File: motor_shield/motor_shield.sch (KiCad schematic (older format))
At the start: 14 parts

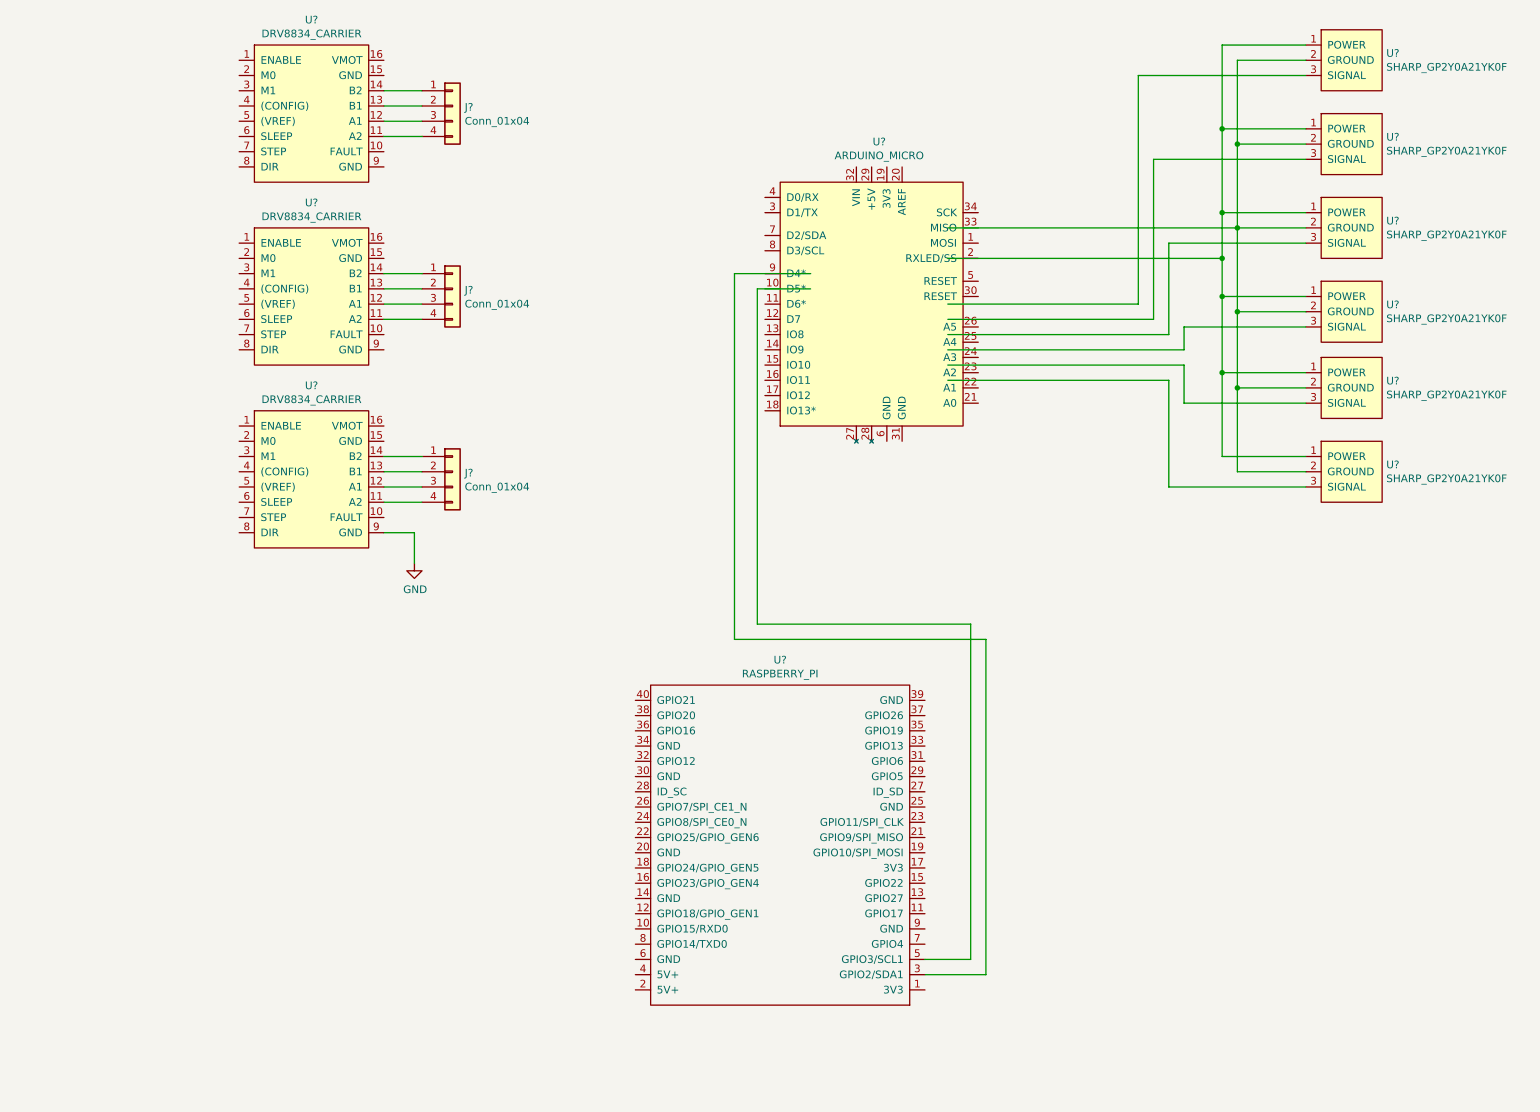
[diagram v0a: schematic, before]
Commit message: Removed buses, wired everything up more simple like
Seemed easier for me to visual the connections w/o the bus lines
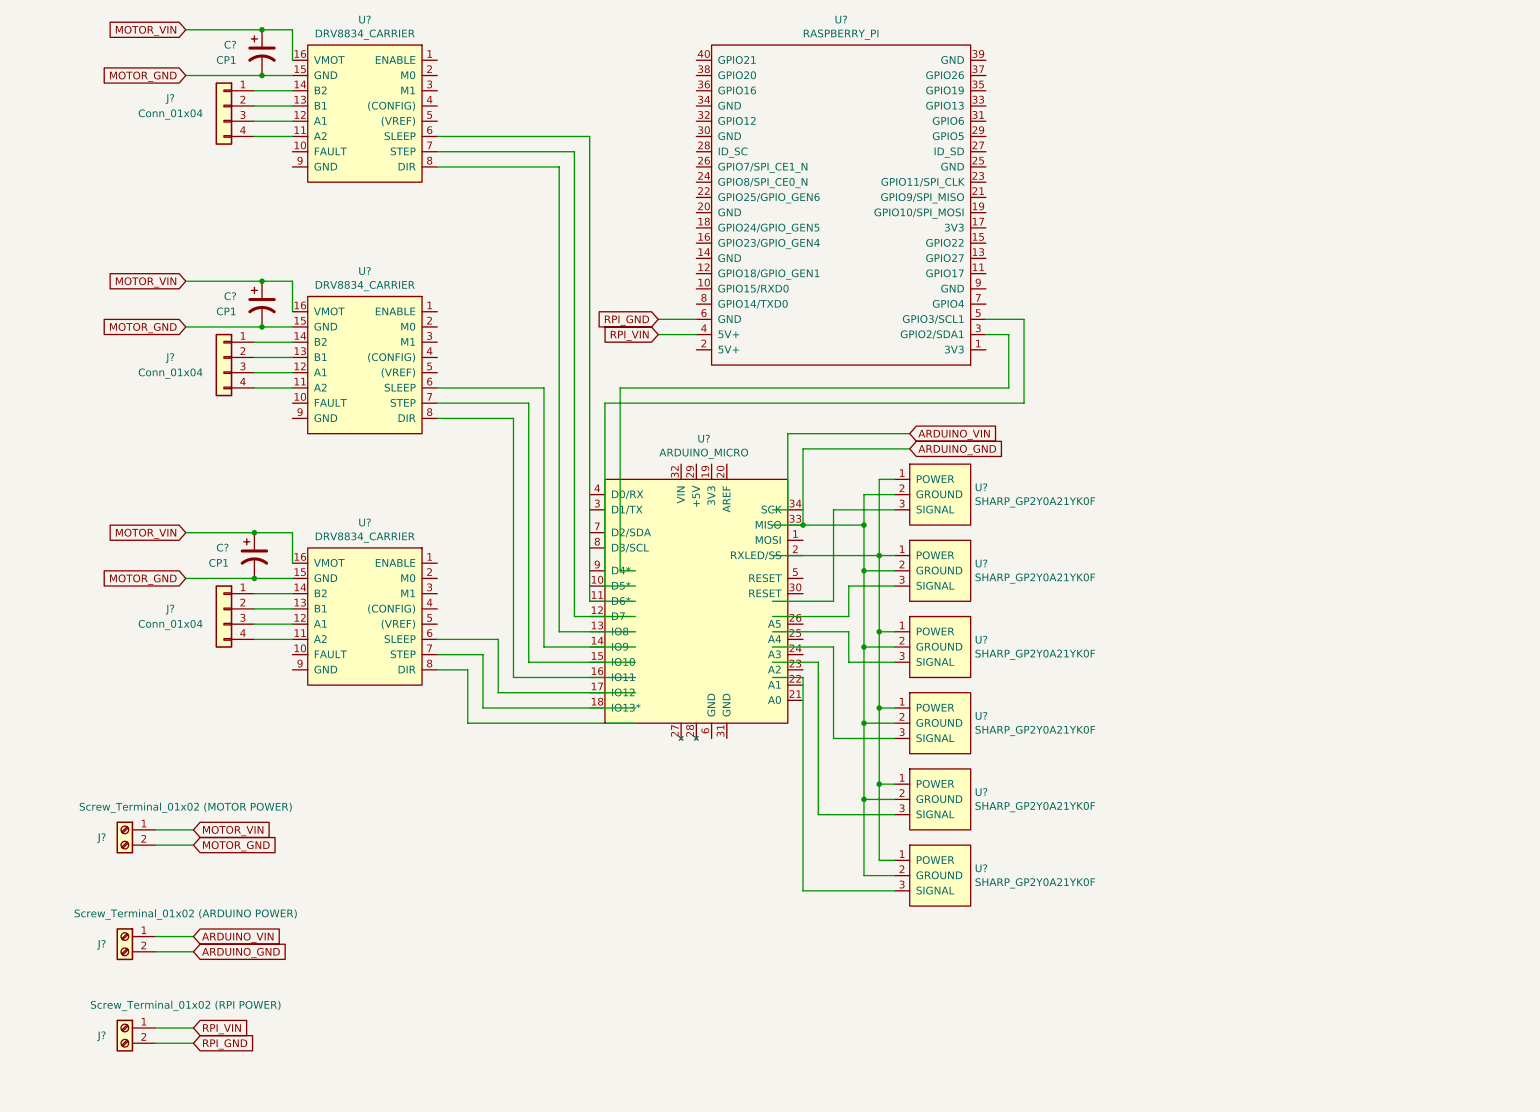
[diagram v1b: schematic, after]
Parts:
- removed J? (x2): Conn_01x04, symbol Connector_Generic:Conn_01x04
- removed U? (x2): DRV8834_CARRIER, symbol CATPOO:DRV8834_CARRIER
- removed U? (x5): SHARP_GP2Y0A21YK0F, symbol CATPOO:SHARP_GP2Y0A21YK0F
- added C? (x3): CP1, symbol Device:CP1
- added J?: Screw_Terminal_01x02 (MOTOR POWER), symbol Connector:Screw_Terminal_01x02
- added J? (x2): Conn_01x04, symbol Connector_Generic:Conn_01x04
- added J?: Screw_Terminal_01x02 (ARDUINO POWER), symbol Connector:Screw_Terminal_01x02
- added J?: Screw_Terminal_01x02 (RPI POWER), symbol Connector:Screw_Terminal_01x02
- added U? (x5): SHARP_GP2Y0A21YK0F, symbol CATPOO:SHARP_GP2Y0A21YK0F
- added U? (x2): DRV8834_CARRIER, symbol CATPOO:DRV8834_CARRIER
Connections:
- net labels added: ARDUINO_GND, ARDUINO_VIN, MOTOR_GND, MOTOR_VIN, RPI_GND, RPI_VIN
- net labels removed: GND
- wire segments 67 -> 121
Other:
- moved on the sheet: J?, U?

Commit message: Assigned footprints, ERC clean up
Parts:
- removed J?: Screw_Terminal_01x02 (ARDUINO POWER), symbol Connector:Screw_Terminal_01x02
- removed J?: Screw_Terminal_01x02 (RPI POWER), symbol Connector:Screw_Terminal_01x02
- removed U? (x4): SHARP_GP2Y0A21YK0F, symbol CATPOO:SHARP_GP2Y0A21YK0F
- added C4: CP1, Capacitor_THT:CP_Radial_D10.0mm_P5.00mm, symbol Device:CP1
- added C5: CP1_Small, Capacitor_THT:CP_Radial_D5.0mm_P2.50mm, symbol Device:CP1_Small
- added J2, J3: Screw_Terminal_01x02, CATPOO:TerminalBlock_Pololu-2_P5.00mm, symbol Connector:Screw_Terminal_01x02
- added U10, U11, U8, U9: SHARP_GP2Y0A21YK0F, Connector_JST:JST_XH_B03B-XH-A_1x03_P2.50mm_Vertical, symbol CATPOO:SHARP_GP2Y0A21YK0F
- C1, C2, C3: renamed from C?; footprint (none) -> Capacitor_THT:CP_Radial_D10.0mm_P5.00mm
- J1: renamed from J?; value Screw_Terminal_01x02 (MOTOR POWER) -> Screw_Terminal_01x02; footprint (none) -> CATPOO:TerminalBlock_Pololu-2_P5.00mm
- J4, J5, J6: renamed from J?; footprint (none) -> Connector_JST:JST_XH_B04B-XH-A_1x04_P2.50mm_Vertical
- U1, U2, U3: renamed from U?; footprint (none) -> CATPOO:DRV8834
- U4: renamed from U?; footprint (none) -> CATPOO:DIP-34_600
- U5: renamed from U?; footprint (none) -> Connector_PinHeader_2.54mm:PinHeader_2x20_P2.54mm_Vertical
- U6, U7: renamed from U?; footprint (none) -> Connector_JST:JST_XH_B03B-XH-A_1x03_P2.50mm_Vertical
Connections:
- net labels added: +5V, +7.5V, GND
- wire segments 121 -> 145
- no-connect marks 0 -> 65
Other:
- moved on the sheet: J1, U5, U6, U7

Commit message: WIP board layout
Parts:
- C1: renamed from C2; footprint Capacitor_THT:CP_Radial_D10.0mm_P5.00mm -> Capacitor_THT:CP_Radial_D8.0mm_P3.50mm
- C2: renamed from C3; value CP1 -> CP2; footprint Capacitor_THT:CP_Radial_D10.0mm_P5.00mm -> Capacitor_THT:CP_Radial_D8.0mm_P3.50mm
- C3: renamed from C1; value CP1 -> CP3; footprint Capacitor_THT:CP_Radial_D10.0mm_P5.00mm -> Capacitor_THT:CP_Radial_D8.0mm_P3.50mm
- C4: footprint Capacitor_THT:CP_Radial_D10.0mm_P5.00mm -> Capacitor_THT:CP_Radial_D8.0mm_P2.50mm
- U4: footprint CATPOO:DIP-34_600 -> CATPOO:ARDUINO_MICRO
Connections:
- net labels removed: +5V, +7.5V
- wire segments 145 -> 136
- no-connect marks 65 -> 66
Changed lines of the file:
@@
 EESchema Schematic File Version 4
+LIBS:motor_shield-cache
 EELAYER 26 0
 EELAYER END
@@
 F 0 "U4" H 4750 5615 50  0000 C CNN
 F 1 "ARDUINO_MICRO" H 4750 5524 50  0000 C CNN
-F 2 "CATPOO:DIP-34_600" H 4750 4550 50  0001 C CNN
+F 2 "CATPOO:ARDUINO_MICRO" H 4750 4550 50  0001 C CNN
 F 3 "" H 4750 4550 50  0001 C CNN
 	1    4750 4550
@@
 $EndComp
 $Comp
-L Device:CP1 C2
+L Device:CP1 C1
 U 1 1 5C82394E
 P 1850 950
-F 0 "C2" H 1600 1000 50  0000 L CNN
+F 0 "C1" H 1600 1000 50  0000 L CNN
 F 1 "CP1" H 1550 900 50  0000 L CNN
-F 2 "Capacitor_THT:CP_Radial_D10.0mm_P5.00mm" H 1850 950 50  0001 C CNN
+F 2 "Capacitor_THT:CP_Radial_D8.0mm_P3.50mm" H 1850 950 50  0001 C CNN
 F 3 "~" H 1850 950 50  0001 C CNN
 	1    1850 950
@@
 $EndComp
 $Comp
-L Device:CP1 C3
+L Device:CP1 C2
 U 1 1 5C837FE6
 P 1850 2600
-F 0 "C3" H 1600 2650 50  0000 L CNN
-F 1 "CP1" H 1550 2550 50  0000 L CNN
-F 2 "Capacitor_THT:CP_Radial_D10.0mm_P5.00mm" H 1850 2600 50  0001 C CNN
+F 0 "C2" H 1600 2650 50  0000 L CNN
+F 1 "CP2" H 1550 2550 50  0000 L CNN
+F 2 "Capacitor_THT:CP_Radial_D8.0mm_P3.50mm" H 1850 2600 50  0001 C CNN
 F 3 "~" H 1850 2600 50  0001 C CNN
 	1    1850 2600
@@
 $EndComp
 $Comp
-L Device:CP1 C1
+L Device:CP1 C3
 U 1 1 5C83805A
 P 1800 4250
-F 0 "C1" H 1550 4300 50  0000 L CNN
-F 1 "CP1" H 1500 4200 50  0000 L CNN
-F 2 "Capacitor_THT:CP_Radial_D10.0mm_P5.00mm" H 1800 4250 50  0001 C CNN
+F 0 "C3" H 1550 4300 50  0000 L CNN
+F 1 "CP3" H 1500 4200 50  0000 L CNN
+F 2 "Capacitor_THT:CP_Radial_D8.0mm_P3.50mm" H 1800 4250 50  0001 C CNN
 F 3 "~" H 1800 4250 50  0001 C CNN
 	1    1800 4250
@@
 	1850 2450 1350 2450
 Connection ~ 1850 2450
+Text GLabel 1400 6800 3    50   Input ~ 0
+MOTOR_VIN
 Text GLabel 1300 6800 3    50   Input ~ 0
-MOTOR_VIN
-Text GLabel 1400 6800 3    50   Input ~ 0
 MOTOR_GND
+Text GLabel 3100 6800 3    50   Input ~ 0
+ARDUINO_VIN
 Text GLabel 3000 6800 3    50   Input ~ 0
-ARDUINO_VIN
-Text GLabel 3100 6800 3    50   Input ~ 0
 ARDUINO_GND
 Text GLabel 6100 3450 2    50   Input ~ 0
@@
 Wire Wire Line
 	5600 3450 5600 4050
+Text GLabel 4800 6800 3    50   Input ~ 0
+RPI_VIN
 Text GLabel 4700 6800 3    50   Input ~ 0
-RPI_VIN
-Text GLabel 4800 6800 3    50   Input ~ 0
 RPI_GND
 Text GLabel 4450 2800 0    50   Input ~ 0
@@
 F 0 "C4" H 4800 2900 50  0000 L CNN
 F 1 "CP1" H 4800 2450 50  0000 L CNN
-F 2 "Capacitor_THT:CP_Radial_D10.0mm_P5.00mm" H 4850 2650 50  0001 C CNN
+F 2 "Capacitor_THT:CP_Radial_D8.0mm_P2.50mm" H 4850 2650 50  0001 C CNN
 F 3 "~" H 4850 2650 50  0001 C CNN
 	1    4850 2650
@@
 Wire Wire Line
 	4650 2500 4850 2500
-$Comp
-L power:GND #PWR0103
-U 1 1 5CA8F279
-P 1550 6650
-F 0 "#PWR0103" H 1550 6400 50  0001 C CNN
-F 1 "GND" H 1555 6477 50  0000 C CNN
-F 2 "" H 1550 6650 50  0001 C CNN
-F 3 "" H 1550 6650 50  0001 C CNN
-	1    1550 6650
-	1    0    0    -1
-$EndComp
-$Comp
-L power:+7.5V #PWR0105
-U 1 1 5CA9E4FA
-P 1100 6650
-F 0 "#PWR0105" H 1100 6500 50  0001 C CNN
-F 1 "+7.5V" H 1115 6823 50  0000 C CNN
-F 2 "" H 1100 6650 50  0001 C CNN
-F 3 "" H 1100 6650 50  0001 C CNN
-	1    1100 6650
-	1    0    0    -1
-$EndComp
-$Comp
-L power:+5V #PWR0106
-U 1 1 5CAA3A9E
-P 4500 6650
-F 0 "#PWR0106" H 4500 6500 50  0001 C CNN
-F 1 "+5V" H 4515 6823 50  0000 C CNN
-F 2 "" H 4500 6650 50  0001 C CNN
-F 3 "" H 4500 6650 50  0001 C CNN
-	1    4500 6650
-	1    0    0    -1
-$EndComp
 $Comp
 L power:GND #PWR0107
@@
 NoConn ~ 3000 4300
 NoConn ~ 5150 2900
-$Comp
-L power:PWR_FLAG #FLG0102
-U 1 1 5CD0B3E5
-P 800 6650
-F 0 "#FLG0102" H 800 6725 50  0001 C CNN
-F 1 "PWR_FLAG" H 800 6824 50  0000 C CNN
-F 2 "" H 800 6650 50  0001 C CNN
-F 3 "~" H 800 6650 50  0001 C CNN
-	1    800  6650
-	1    0    0    -1
-$EndComp
 NoConn ~ 7050 2600
-Wire Wire Line
-	1550 6650 1400 6650
-Wire Wire Line
-	1300 6650 1100 6650
-Wire Wire Line
-	1100 6650 800  6650
-Connection ~ 1100 6650
-Wire Wire Line
-	1400 6800 1400 6650
-Connection ~ 1400 6650
-Wire Wire Line
-	1300 6800 1300 6650
-Connection ~ 1300 6650
 $Comp
 L Connector:Screw_Terminal_01x02 J2
@@
 	0    1    -1   0
 $EndComp
-$Comp
-L power:GND #PWR02
-U 1 1 5CDAA99A
-P 3250 6650
-F 0 "#PWR02" H 3250 6400 50  0001 C CNN
-F 1 "GND" H 3255 6477 50  0000 C CNN
-F 2 "" H 3250 6650 50  0001 C CNN
-F 3 "" H 3250 6650 50  0001 C CNN
-	1    3250 6650
-	1    0    0    -1
-$EndComp
-$Comp
-L power:+7.5V #PWR01
-U 1 1 5CDAA9A0
-P 2800 6650
-F 0 "#PWR01" H 2800 6500 50  0001 C CNN
-F 1 "+7.5V" H 2815 6823 50  0000 C CNN
-F 2 "" H 2800 6650 50  0001 C CNN
-F 3 "" H 2800 6650 50  0001 C CNN
-	1    2800 6650
-	1    0    0    -1
-$EndComp
-$Comp
-L power:PWR_FLAG #FLG01
-U 1 1 5CDAA9A6
-P 2500 6650
-F 0 "#FLG01" H 2500 6725 50  0001 C CNN
-F 1 "PWR_FLAG" H 2500 6824 50  0000 C CNN
-F 2 "" H 2500 6650 50  0001 C CNN
-F 3 "~" H 2500 6650 50  0001 C CNN
-	1    2500 6650
-	1    0    0    -1
-$EndComp
-Wire Wire Line
-	3250 6650 3100 6650
-Wire Wire Line
-	3000 6650 2800 6650
-Wire Wire Line
-	2800 6650 2500 6650
-Connection ~ 2800 6650
-Wire Wire Line
-	3100 6800 3100 6650
-Connection ~ 3100 6650
-Wire Wire Line
-	3000 6800 3000 6650
-Connection ~ 3000 6650
+NoConn ~ 5200 4150
 $Comp
 L Connector:Screw_Terminal_01x02 J3
@@
 	0    1    -1   0
 $EndComp
-$Comp
-L power:GND #PWR03
-U 1 1 5CDB16DE
-P 4950 6650
-F 0 "#PWR03" H 4950 6400 50  0001 C CNN
-F 1 "GND" H 4955 6477 50  0000 C CNN
-F 2 "" H 4950 6650 50  0001 C CNN
-F 3 "" H 4950 6650 50  0001 C CNN
-	1    4950 6650
-	1    0    0    -1
-$EndComp
-$Comp
-L power:PWR_FLAG #FLG02
-U 1 1 5CDB16EA
-P 4200 6650
-F 0 "#FLG02" H 4200 6725 50  0001 C CNN
-F 1 "PWR_FLAG" H 4200 6824 50  0000 C CNN
-F 2 "" H 4200 6650 50  0001 C CNN
-F 3 "~" H 4200 6650 50  0001 C CNN
-	1    4200 6650
-	1    0    0    -1
-$EndComp
-Wire Wire Line
-	4950 6650 4800 6650
-Wire Wire Line
-	4800 6800 4800 6650
-Connection ~ 4800 6650
-Wire Wire Line
-	4700 6800 4700 6650
-Connection ~ 4700 6650
-Wire Wire Line
-	4200 6650 4500 6650
-Connection ~ 4500 6650
-Wire Wire Line
-	4500 6650 4700 6650
+Wire Wire Line
+	1300 6650 1300 6800
+Wire Wire Line
+	4800 6650 4800 6800
+Wire Wire Line
+	4700 6650 4700 6800
+Wire Wire Line
+	3100 6650 3100 6800
+Wire Wire Line
+	3000 6650 3000 6800
+Wire Wire Line
+	1400 6650 1400 6800
 $EndSCHEMATC
